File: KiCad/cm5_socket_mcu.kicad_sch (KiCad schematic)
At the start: 3 parts, among them IC1 AZ1117CH2-3.3TRG1

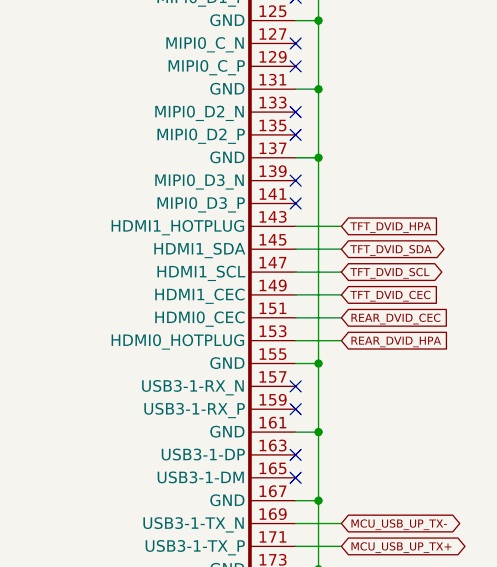
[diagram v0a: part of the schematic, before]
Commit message: CEC and HPD signals fixed
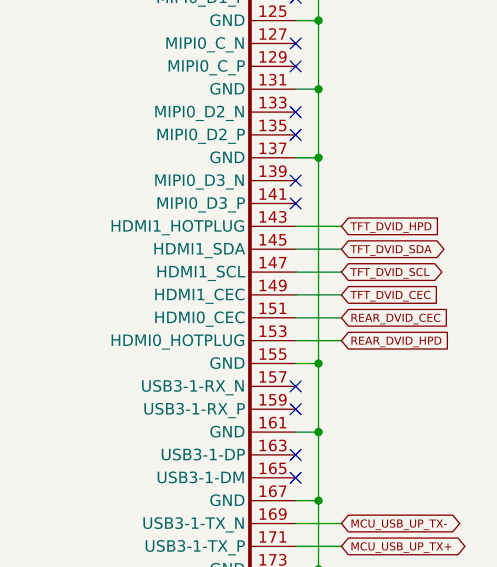
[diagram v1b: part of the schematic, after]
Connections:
- net REAR_DVID_HPA renamed REAR_DVID_HPD
- net TFT_DVID_HPA renamed TFT_DVID_HPD
